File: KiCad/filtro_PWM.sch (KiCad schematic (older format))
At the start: 5 parts

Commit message: adição departe dos footprints
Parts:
- Filtro_Butterworth1: footprint SOP100P600X150-8N -> (none)
- R1, R2, R_Filtro_In-1: footprint (none) -> Resistor_SMD:R_0805_2012Metric
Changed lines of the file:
@@
 $Descr A4 11693 8268
 encoding utf-8
-Sheet 8 9
+Sheet 6 10
 Title ""
 Date ""
@@
 F 0 "Filtro_Butterworth1" H 5750 3365 50  0000 C CNN
 F 1 "LM358" H 5750 3274 50  0000 C CNN
-F 2 "SOP100P600X150-8N" H 6150 3200 50  0001 L CNN
+F 2 "" H 6150 3200 50  0001 L CNN
 F 3 "https://www.onsemi.com/pdf/datasheet/lm358-d.pdf" H 6150 3100 50  0001 L CNN
 F 4 "Operational Amplifiers SOP-8 RoHS" H 6150 3000 50  0001 L CNN "Description"
@@
 F 0 "R_Filtro_In-1" H 4418 3346 50  0000 L CNN
 F 1 "R_US" H 4418 3255 50  0000 L CNN
-F 2 "" V 4390 3290 50  0001 C CNN
+F 2 "Resistor_SMD:R_0805_2012Metric" V 4390 3290 50  0001 C CNN
 F 3 "~" H 4350 3300 50  0001 C CNN
 	1    4350 3300
@@
 F 0 "R2" H 5118 2946 50  0000 L CNN
 F 1 "R_FB" H 5118 2855 50  0000 L CNN
-F 2 "" V 5090 2890 50  0001 C CNN
+F 2 "Resistor_SMD:R_0805_2012Metric" V 5090 2890 50  0001 C CNN
 F 3 "~" H 5050 2900 50  0001 C CNN
 	1    5050 2900
@@
 F 0 "R1" H 4618 2946 50  0000 L CNN
 F 1 "R_Filtro_In+" H 4618 2855 50  0000 L CNN
-F 2 "" V 4590 2890 50  0001 C CNN
+F 2 "Resistor_SMD:R_0805_2012Metric" V 4590 2890 50  0001 C CNN
 F 3 "~" H 4550 2900 50  0001 C CNN
 	1    4550 2900

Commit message: pble_zip
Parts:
- C_GND_Filtro1: value C -> 10nF; footprint (none) -> Capacitor_SMD:C_0805_2012Metric_Pad1.18x1.45mm_HandSolder
- Filtro_Butterworth1: footprint (none) -> Package_SO:SOIC-8_3.9x4.9mm_P1.27mm
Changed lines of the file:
@@
 F 0 "Filtro_Butterworth1" H 5750 3365 50  0000 C CNN
 F 1 "LM358" H 5750 3274 50  0000 C CNN
-F 2 "" H 6150 3200 50  0001 L CNN
+F 2 "Package_SO:SOIC-8_3.9x4.9mm_P1.27mm" H 6150 3200 50  0001 L CNN
 F 3 "https://www.onsemi.com/pdf/datasheet/lm358-d.pdf" H 6150 3100 50  0001 L CNN
 F 4 "Operational Amplifiers SOP-8 RoHS" H 6150 3000 50  0001 L CNN "Description"
@@
 P 4550 3450
 F 0 "C_GND_Filtro1" H 4665 3496 50  0000 L CNN
-F 1 "C" H 4665 3405 50  0000 L CNN
-F 2 "" H 4588 3300 50  0001 C CNN
+F 1 "10nF" H 4665 3405 50  0000 L CNN
+F 2 "Capacitor_SMD:C_0805_2012Metric_Pad1.18x1.45mm_HandSolder" H 4588 3300 50  0001 C CNN
 F 3 "~" H 4550 3450 50  0001 C CNN
 	1    4550 3450

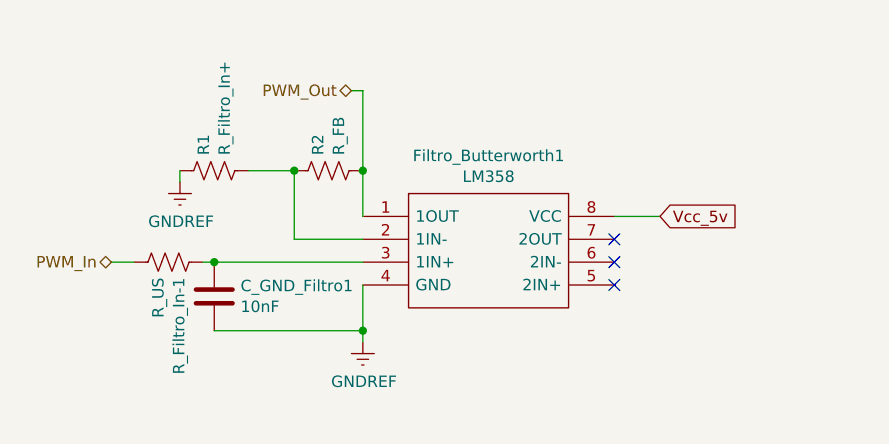
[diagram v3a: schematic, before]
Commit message: correção P1: LCD e Capacitores
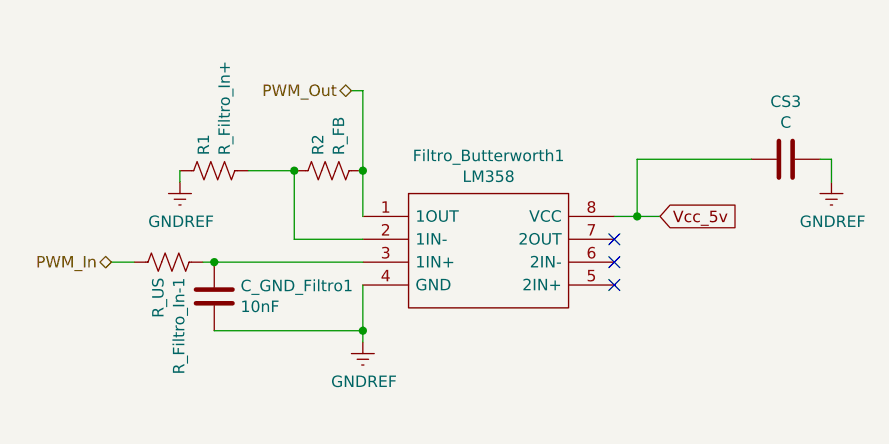
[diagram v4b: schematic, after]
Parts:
- added CS3: C, Capacitor_SMD:C_0805_2012Metric_Pad1.18x1.45mm_HandSolder, symbol Device:C
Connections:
- net GNDREF: now also CS3.1
- net Vcc_5v: now also CS3.2
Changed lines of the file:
@@
 Vcc_5v
 Wire Wire Line
-	6500 3100 6300 3100
+	6500 3100 6400 3100
 $Comp
 L power:GNDREF #PWR0127
@@
 Wire Wire Line
 	4100 3300 4200 3300
+$Comp
+L power:GNDREF #PWR?
+U 1 1 60FB4277
+P 7250 2950
+AR Path="/60FB4277" Ref="#PWR?"  Part="1"
+AR Path="/60B33116/60FB4277" Ref="#PWR04"  Part="1"
+F 0 "#PWR04" H 7250 2700 50  0001 C CNN
+F 1 "GNDREF" H 7255 2777 50  0000 C CNN
+F 2 "" H 7250 2950 50  0001 C CNN
+F 3 "" H 7250 2950 50  0001 C CNN
+	1    7250 2950
+	1    0    0    -1
+$EndComp
+$Comp
+L Device:C CS?
+U 1 1 60FB427D
+P 7050 2850
+AR Path="/60FB427D" Ref="CS?"  Part="1"
+AR Path="/60B33116/60FB427D" Ref="CS3"  Part="1"
+F 0 "CS3" V 6798 2850 50  0000 C CNN
+F 1 "C" V 6889 2850 50  0000 C CNN
+F 2 "Capacitor_SMD:C_0805_2012Metric_Pad1.18x1.45mm_HandSolder" H 7088 2700 50  0001 C CNN
+F 3 "~" H 7050 2850 50  0001 C CNN
+	1    7050 2850
+	0    1    1    0
+$EndComp
+Wire Wire Line
+	7250 2950 7250 2850
+Wire Wire Line
+	7250 2850 7200 2850
+Wire Wire Line
+	6900 2850 6400 2850
+Wire Wire Line
+	6400 2850 6400 3100
+Connection ~ 6400 3100
+Wire Wire Line
+	6400 3100 6300 3100
 $EndSCHEMATC

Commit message: Valores dos capacitores CS
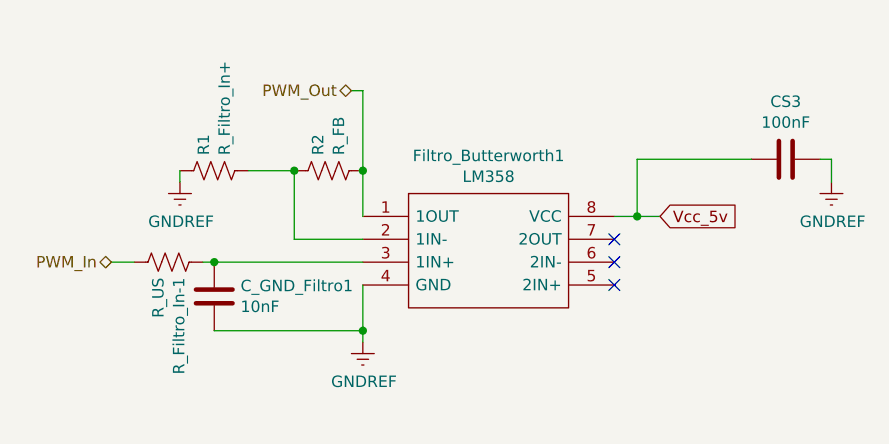
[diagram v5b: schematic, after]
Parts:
- CS3: value C -> 100nF
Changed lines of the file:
@@
 AR Path="/60B33116/60FB427D" Ref="CS3"  Part="1"
 F 0 "CS3" V 6798 2850 50  0000 C CNN
-F 1 "C" V 6889 2850 50  0000 C CNN
+F 1 "100nF" V 6889 2850 50  0000 C CNN
 F 2 "Capacitor_SMD:C_0805_2012Metric_Pad1.18x1.45mm_HandSolder" H 7088 2700 50  0001 C CNN
 F 3 "~" H 7050 2850 50  0001 C CNN

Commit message: Rbutterworth
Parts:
- R1: value R_Filtro_In+ -> 10
- R2: value R_FB -> 51k
- R_Filtro_In-1: value R_US -> 10k
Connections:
- net PWM_Out: now also R2.1; no longer R2.2
- net at Filtro_Butterworth1.2 (1IN-), R1.2: now also R2.2; no longer R2.1
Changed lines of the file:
@@
 P 4350 3300
 F 0 "R_Filtro_In-1" H 4418 3346 50  0000 L CNN
-F 1 "R_US" H 4418 3255 50  0000 L CNN
+F 1 "10k" H 4418 3255 50  0000 L CNN
 F 2 "Resistor_SMD:R_0805_2012Metric" V 4390 3290 50  0001 C CNN
 F 3 "~" H 4350 3300 50  0001 C CNN
@@
 P 5050 2900
 F 0 "R2" H 5118 2946 50  0000 L CNN
-F 1 "R_FB" H 5118 2855 50  0000 L CNN
+F 1 "51k" H 5118 2855 50  0000 L CNN
 F 2 "Resistor_SMD:R_0805_2012Metric" V 5090 2890 50  0001 C CNN
 F 3 "~" H 5050 2900 50  0001 C CNN
 	1    5050 2900
-	0    -1   -1   0
+	0    1    1    0
 $EndComp
 $Comp
@@
 P 4550 2900
 F 0 "R1" H 4618 2946 50  0000 L CNN
-F 1 "R_Filtro_In+" H 4618 2855 50  0000 L CNN
+F 1 "10" H 4618 2855 50  0000 L CNN
 F 2 "Resistor_SMD:R_0805_2012Metric" V 4590 2890 50  0001 C CNN
 F 3 "~" H 4550 2900 50  0001 C CNN
